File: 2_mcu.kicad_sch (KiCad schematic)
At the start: 27 parts, among them J1 SWD TagConnect

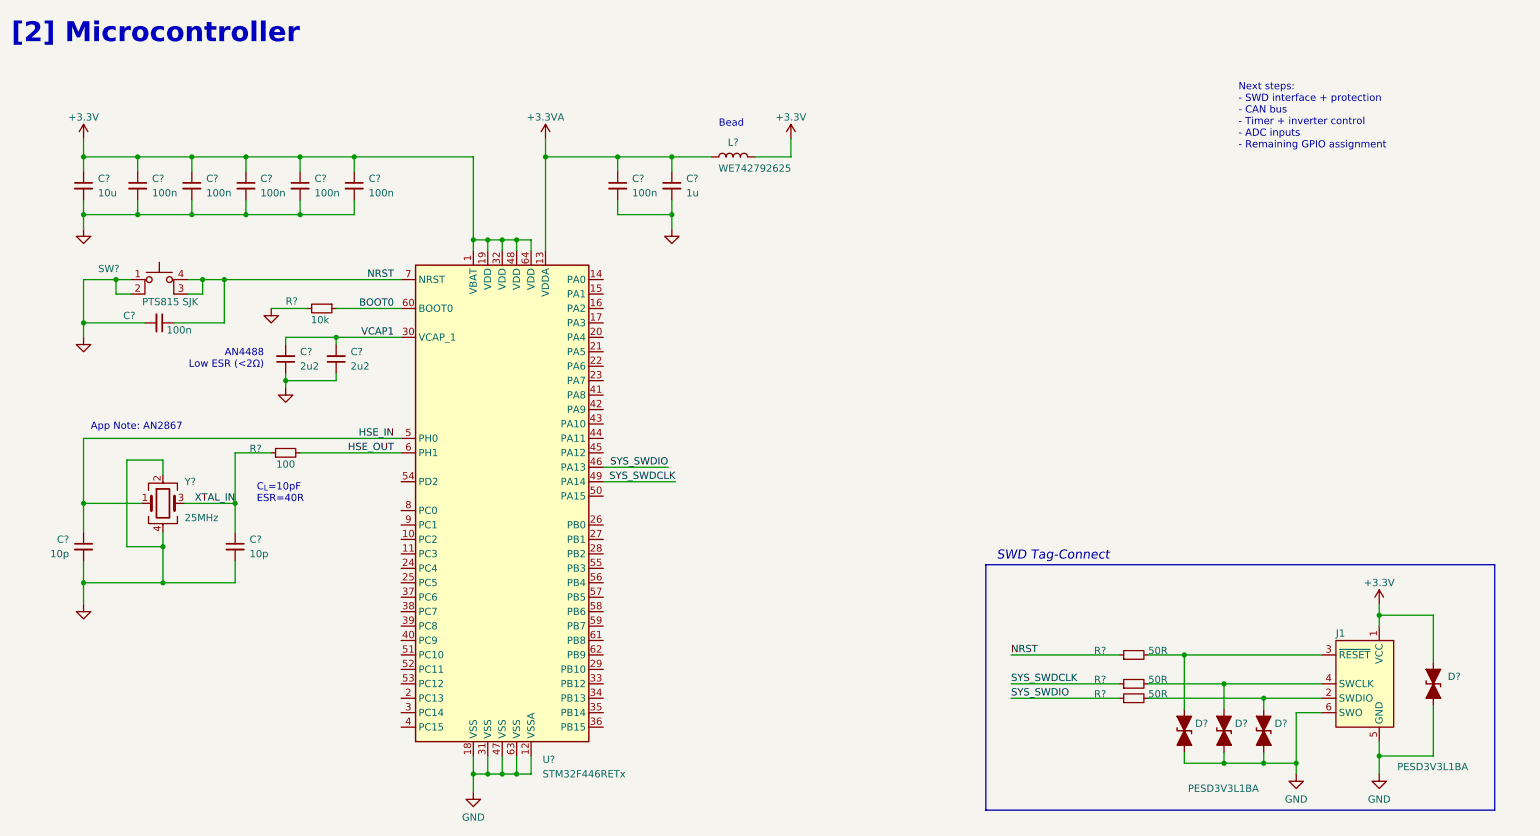
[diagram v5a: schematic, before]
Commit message: global labels to local labels wherever possible and mcu pinout addition
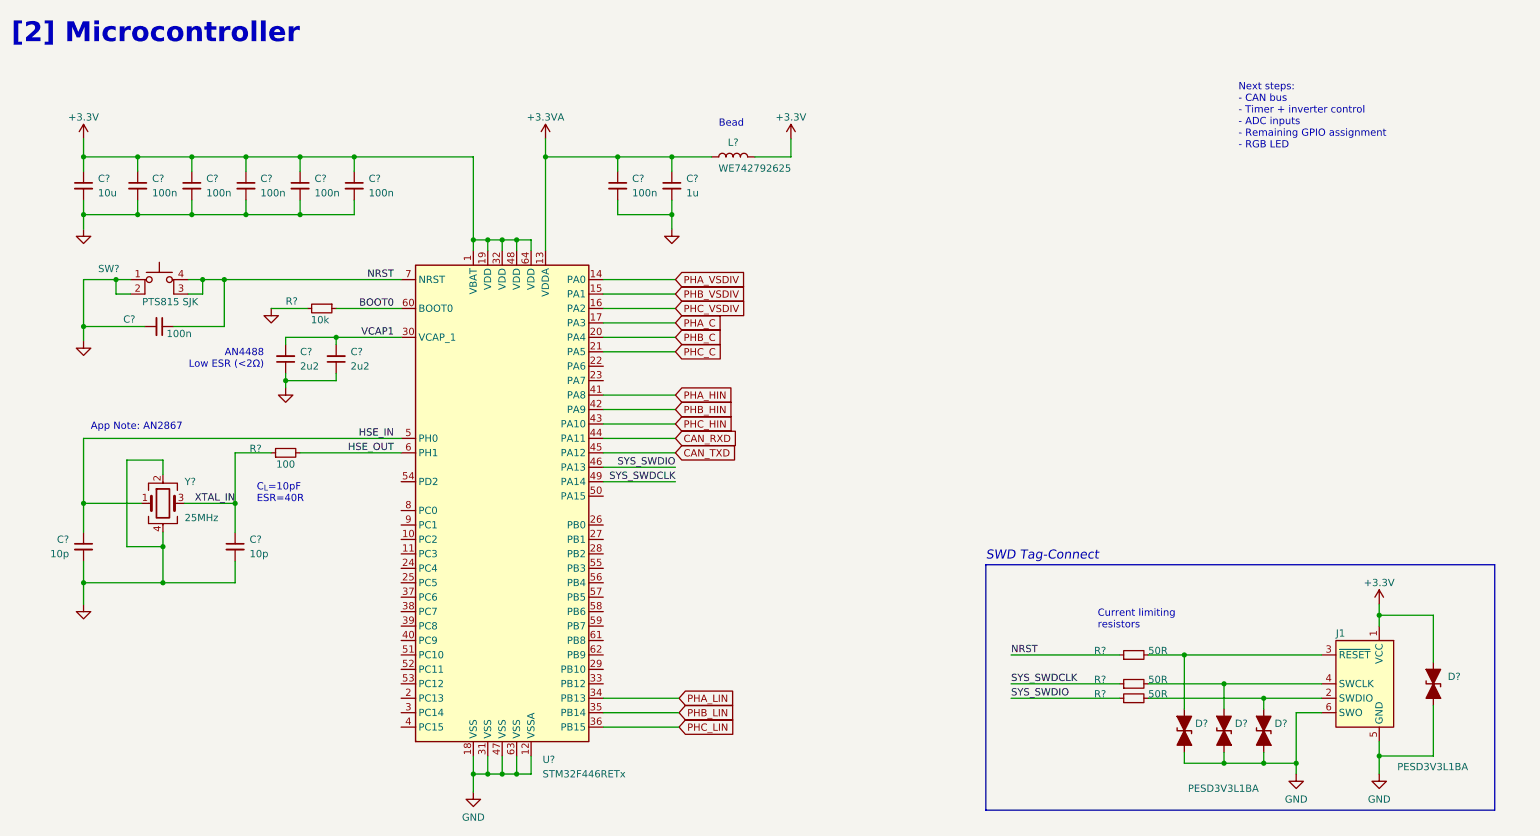
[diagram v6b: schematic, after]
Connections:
- net PHA_VSDIV: now reaches U?.14 (PA0)
- net PHB_VSDIV: now reaches U?.15 (PA1)
- net PHC_VSDIV: now reaches U?.16 (PA2)
- net PHA_C: now reaches U?.17 (PA3)
- net PHB_C: now reaches U?.20 (PA4)
- net PHC_C: now reaches U?.21 (PA5)
- net PHA_LIN: now reaches U?.34 (PB13)
- net PHB_LIN: now reaches U?.35 (PB14)
- net PHC_LIN: now reaches U?.36 (PB15)
- net PHA_HIN: now reaches U?.41 (PA8)
- net PHB_HIN: now reaches U?.42 (PA9)
- net PHC_HIN: now reaches U?.43 (PA10)
- net CAN_RXD: now reaches U?.44 (PA11)
- net CAN_TXD: now reaches U?.45 (PA12)
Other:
- note added: "Current limiting resistors"
- note added: "Next steps: - CAN bus - Timer + inverter control - ADC inputs - Remaining GPIO assignment - RGB LED"
- note removed: "Next steps: - SWD interface + protection - CAN bus - Timer + inverter control - ADC inputs - Remaining GPIO assignment"
- moved on the sheet: C?

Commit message: todo list update
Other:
- note added: "Next steps: - CAN bus - Timer + inverter control - ADC inputs - Remaining GPIO assignment - RGB LED - Thermistor in phase design"
- note removed: "Next steps: - CAN bus - Timer + inverter control - ADC inputs - Remaining GPIO assignment - RGB LED"
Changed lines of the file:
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@@
     (effects (font (size 1.6 1.6) italic) (justify left bottom))
   )
-  (text "Next steps:\n- CAN bus\n- Timer + inverter control\n- ADC inputs\n- Remaining GPIO assignment\n- RGB LED"
+  (text "Next steps:\n- CAN bus\n- Timer + inverter control\n- ADC inputs\n- Remaining GPIO assignment\n- RGB LED\n- Thermistor in phase design"
     (at 234.315 43.815 0)
     (effects (font (size 1.27 1.27)) (justify left bottom))

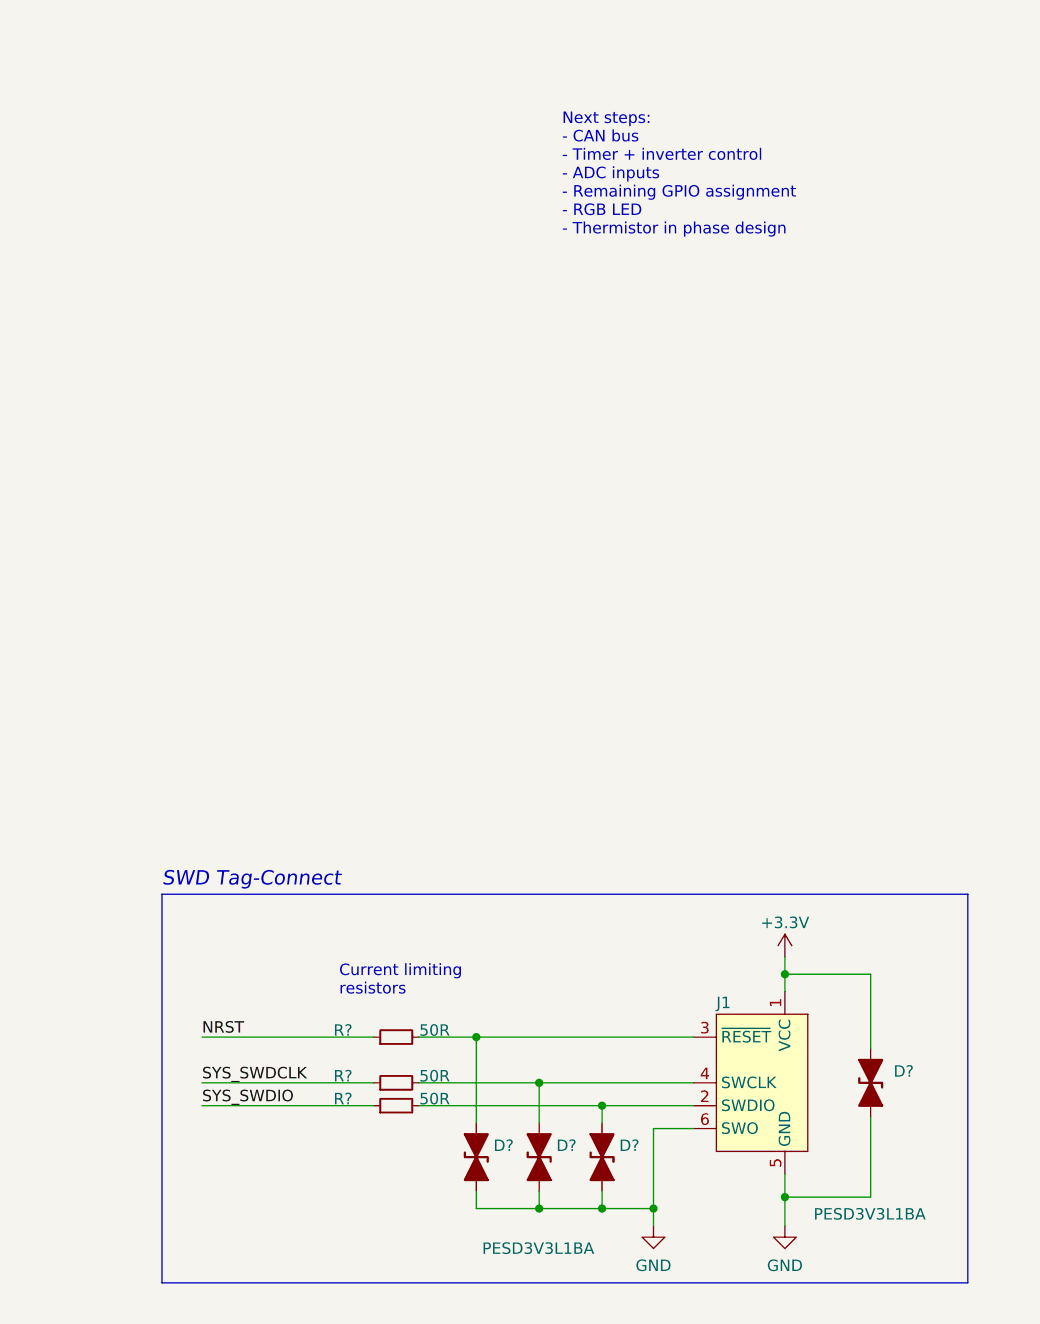
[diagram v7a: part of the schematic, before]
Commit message: check ESD protection for CAN and SWD bus
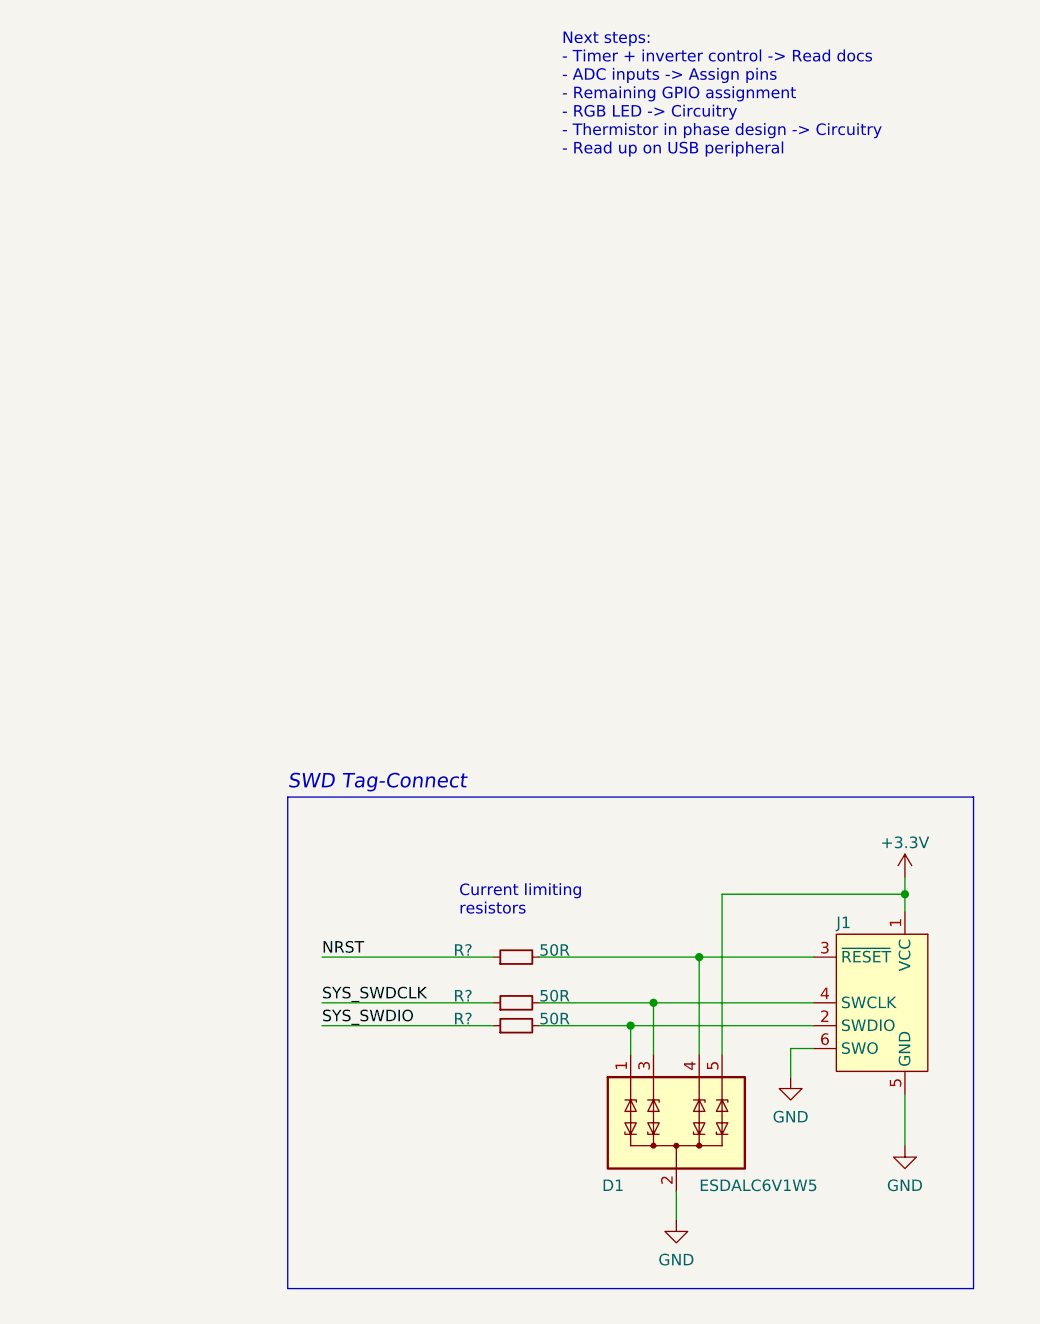
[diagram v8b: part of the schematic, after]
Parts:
- removed D? (x4): PESD3V3L1BA, Diode_SMD:D_SOD-323_HandSoldering, symbol Device:D_TVS_Filled
- added D1: ESDALC6V1W5, symbol Power_Protection:ESDALC6V1W5
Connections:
- net +3.3V: now also D1.5 (TVS4)
- net GND: now also D1.2 (COM)
- net at J1.4 (SWCLK), R?.2: now also D1.3 (TVS2)
- net at J1.2 (SWDIO), R?.2: now also D1.1 (TVS1)
- net at J1.3 (~{RESET}), R?.2: now also D1.4 (TVS3)
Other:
- note added: "Next steps: - Timer + inverter control -> Read docs - ADC inputs -> Assign pins - Remaining GPIO assignment - RGB LED -> Circuitry - Thermistor in phase design -> Circuitry - Read up on USB peripheral"
- note removed: "Next steps: - CAN bus - Timer + inverter control - ADC inputs - Remaining GPIO assignment - RGB LED - Thermistor in phase design"
- moved on the sheet: J1, R?
